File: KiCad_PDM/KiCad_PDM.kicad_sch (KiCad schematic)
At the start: 67 parts, among them J1 Conn_02x16_Top_Bottom, J2 6437288-1, J3 T66145145-1500, U1 74HC27D, U2 74HC27D, U3 74HC27D, U4 74HC27D, U5 KF33BDT-TR

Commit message: Added TS/Souce connections, fixed flyback diode connections, fixed current sense kelvin connections
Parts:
- added C57, C58: C_Polarized, Capacitor_THT:CP_Radial_D8.0mm_P2.50mm, symbol Device:C_Polarized
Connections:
- net +BATT: now also C57.1, C58.1
- net GND: now also C57.2, C58.2
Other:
- note added: "Bulk Decoupling"

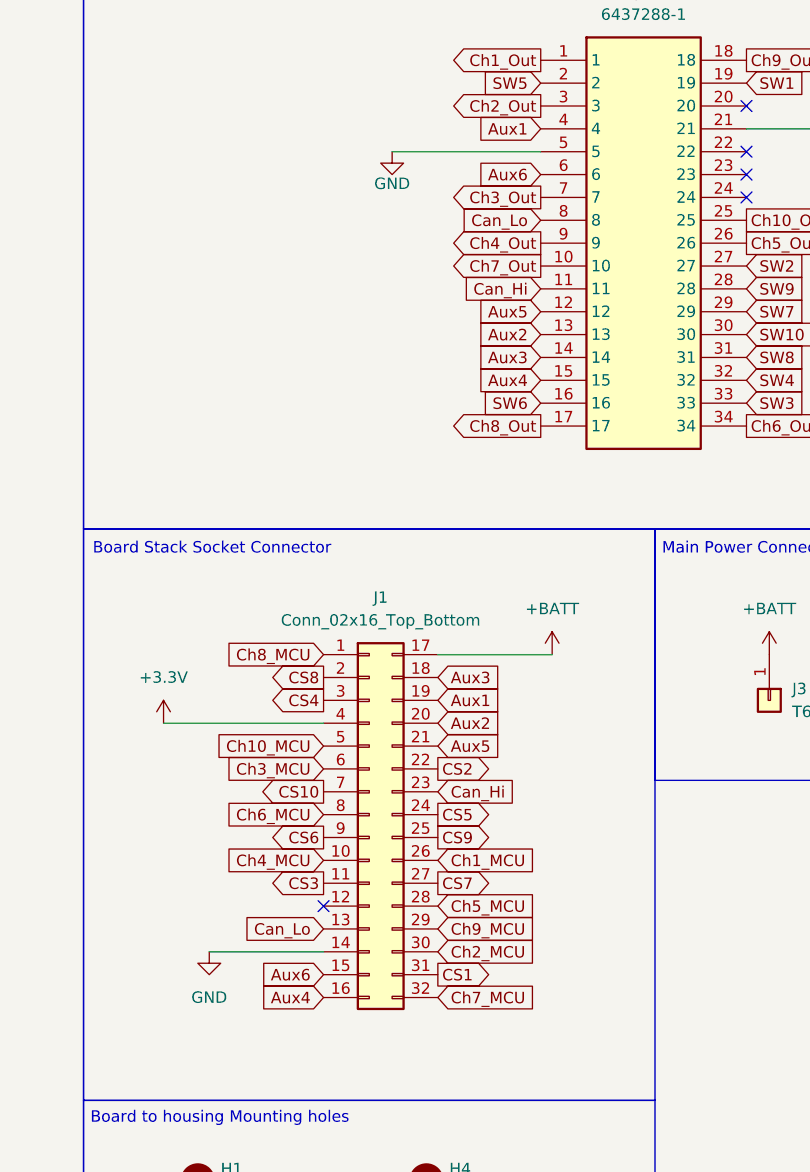
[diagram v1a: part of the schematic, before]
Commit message: fixed CAN trace routing (diff pair), reduced digital signal trace size to 0.2mm
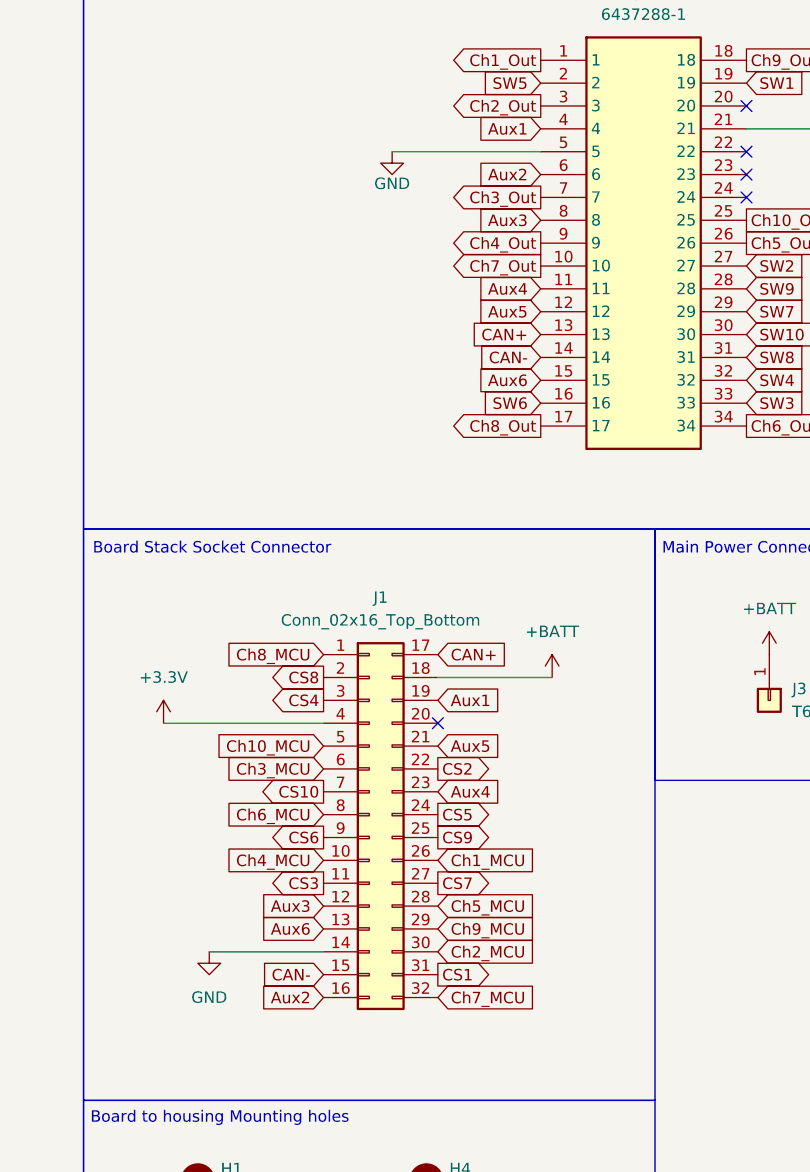
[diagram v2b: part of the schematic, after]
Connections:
- net Can_Hi is gone; now on net Aux4: J1.23 (Pin_23), J2.11
- net +BATT: now also J1.18 (Pin_18); no longer J1.17 (Pin_17)
- net Aux2: now also J1.16 (Pin_16), J2.6; no longer J1.20 (Pin_20), J2.13
- net Aux3: now also J1.12 (Pin_12), J2.8; no longer J1.18 (Pin_18), J2.14
- net Aux4: no longer J1.16 (Pin_16), J2.15
- net Aux6: now also J1.13 (Pin_13), J2.15; no longer J1.15 (Pin_15), J2.6
- removed net Can_Lo: J1.13 (Pin_13), J2.8
- new net CAN+: J1.17 (Pin_17), J2.13
- new net CAN-: J1.15 (Pin_15), J2.14
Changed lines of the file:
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@@
 	)
 	(no_connect
-		(at 293.37 121.92)
+		(at 306.07 101.6)
 	)
 	(no_connect
@@
 	(wire
 		(pts
-			(xy 306.07 93.98) (xy 318.77 93.98)
+			(xy 306.07 96.52) (xy 318.77 96.52)
 		)
 		(stroke
@@
 	(global_label "Aux4"
 		(shape input)
-		(at 293.37 132.08 180)
+		(at 306.07 109.22 0)
 		(fields_autoplaced yes)
 		(effects
@@
 				(size 1.27 1.27)
 			)
-			(justify right)
+			(justify left)
 		)
 		(property "Intersheetrefs" "${INTERSHEET_REFS}"
-			(at 285.9096 132.08 0)
+			(at 313.5304 109.22 0)
 			(hide yes)
 			(show_name no)
@@
 					(size 1.27 1.27)
 				)
-				(justify right)
+				(justify left)
 			)
 		)
@@
 	(global_label "Aux4"
 		(shape input)
-		(at 317.5 63.5 180)
+		(at 317.5 53.34 180)
 		(fields_autoplaced yes)
 		(effects
@@
 		)
 		(property "Intersheetrefs" "${INTERSHEET_REFS}"
-			(at 310.0396 63.5 0)
+			(at 310.0396 53.34 0)
 			(hide yes)
 			(show_name no)
@@
 	(global_label "Aux6"
 		(shape input)
-		(at 317.5 40.64 180)
+		(at 317.5 63.5 180)
 		(fields_autoplaced yes)
 		(effects
@@
 		)
 		(property "Intersheetrefs" "${INTERSHEET_REFS}"
-			(at 310.0396 40.64 0)
+			(at 310.0396 63.5 0)
 			(hide yes)
 			(show_name no)
@@
 	(global_label "Aux2"
 		(shape input)
-		(at 317.5 58.42 180)
+		(at 317.5 40.64 180)
 		(fields_autoplaced yes)
 		(effects
@@
 		)
 		(property "Intersheetrefs" "${INTERSHEET_REFS}"
-			(at 310.0396 58.42 0)
+			(at 310.0396 40.64 0)
 			(hide yes)
 			(show_name no)
@@
 	(global_label "Aux6"
 		(shape input)
-		(at 293.37 129.54 180)
+		(at 293.37 124.46 180)
 		(fields_autoplaced yes)
 		(effects
@@
 		)
 		(property "Intersheetrefs" "${INTERSHEET_REFS}"
-			(at 285.9096 129.54 0)
+			(at 285.9096 124.46 0)
 			(hide yes)
 			(show_name no)
@@
 	(global_label "Aux3"
 		(shape input)
-		(at 317.5 60.96 180)
+		(at 317.5 45.72 180)
 		(fields_autoplaced yes)
 		(effects
@@
 		)
 		(property "Intersheetrefs" "${INTERSHEET_REFS}"
-			(at 310.0396 60.96 0)
+			(at 310.0396 45.72 0)
 			(hide yes)
 			(show_name no)
@@
 	(global_label "Aux2"
 		(shape input)
-		(at 306.07 101.6 0)
+		(at 293.37 132.08 180)
 		(fields_autoplaced yes)
 		(effects
@@
 				(size 1.27 1.27)
 			)
-			(justify left)
+			(justify right)
 		)
 		(property "Intersheetrefs" "${INTERSHEET_REFS}"
-			(at 313.5304 101.6 0)
+			(at 285.9096 132.08 0)
 			(hide yes)
 			(show_name no)
@@
 					(size 1.27 1.27)
 				)
-				(justify left)
+				(justify right)
 			)
 		)
@@
 		)
 	)
-	(global_label "Can_Lo"
+	(global_label "CAN-"
 		(shape input)
-		(at 293.37 124.46 180)
+		(at 293.37 129.54 180)
 		(fields_autoplaced yes)
 		(effects
@@
 		)
 		(property "Intersheetrefs" "${INTERSHEET_REFS}"
-			(at 283.6721 124.46 0)
+			(at 285.1233 129.54 0)
 			(hide yes)
 			(show_name no)
@@
 		)
 	)
-	(global_label "Can_Hi"
+	(global_label "CAN+"
 		(shape input)
-		(at 317.5 53.34 180)
+		(at 317.5 58.42 180)
 		(fields_autoplaced yes)
 		(effects
@@
 		)
 		(property "Intersheetrefs" "${INTERSHEET_REFS}"
-			(at 308.0439 53.34 0)
+			(at 309.2533 58.42 0)
 			(hide yes)
 			(show_name no)
@@
 	(global_label "Aux3"
 		(shape input)
-		(at 306.07 96.52 0)
+		(at 293.37 121.92 180)
 		(fields_autoplaced yes)
 		(effects
@@
 				(size 1.27 1.27)
 			)
-			(justify left)
+			(justify right)
 		)
 		(property "Intersheetrefs" "${INTERSHEET_REFS}"
-			(at 313.5304 96.52 0)
+			(at 285.9096 121.92 0)
 			(hide yes)
 			(show_name no)
@@
 					(size 1.27 1.27)
 				)
-				(justify left)
+				(justify right)
 			)
 		)
@@
 		)
 	)
-	(global_label "Can_Hi"
+	(global_label "CAN+"
 		(shape input)
-		(at 306.07 109.22 0)
+		(at 306.07 93.98 0)
 		(fields_autoplaced yes)
 		(effects
@@
 		)
 		(property "Intersheetrefs" "${INTERSHEET_REFS}"
-			(at 315.5261 109.22 0)
+			(at 314.3167 93.98 0)
 			(hide yes)
 			(show_name no)
@@
 		)
 	)
-	(global_label "Can_Lo"
+	(global_label "CAN-"
 		(shape input)
-		(at 317.5 45.72 180)
+		(at 317.5 60.96 180)
 		(fields_autoplaced yes)
 		(effects
@@
 		)
 		(property "Intersheetrefs" "${INTERSHEET_REFS}"
-			(at 307.8021 45.72 0)
+			(at 309.2533 60.96 0)
 			(hide yes)
 			(show_name no)
@@
 	(symbol
 		(lib_id "power:+BATT")
-		(at 318.77 93.98 0)
+		(at 318.77 96.52 0)
 		(unit 1)
 		(body_style 1)
@@
 		(fields_autoplaced yes)
 		(property "Reference" "#PWR033"
-			(at 318.77 97.79 0)
+			(at 318.77 100.33 0)
 			(hide yes)
 			(show_name no)
@@
 		)
 		(property "Value" "+BATT"
-			(at 318.77 88.9 0)
+			(at 318.77 91.44 0)
 			(show_name no)
 			(do_not_autoplace no)
@@
 		)
 		(property "Footprint" ""
-			(at 318.77 93.98 0)
+			(at 318.77 96.52 0)
 			(hide yes)
 			(show_name no)
@@
 		)
 		(property "Datasheet" ""
-			(at 318.77 93.98 0)
+			(at 318.77 96.52 0)
 			(hide yes)
 			(show_name no)
@@
 		)
 		(property "Description" "Power symbol creates a global label with name \"+BATT\""
-			(at 318.77 93.98 0)
+			(at 318.77 96.52 0)
 			(hide yes)
 			(show_name no)
